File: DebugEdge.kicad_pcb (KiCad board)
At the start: 2 copper layers, 16 x 12 mm, 5 parts, among them J1 Upstream Host Connector, J2 DebugEdge_02x05, J3 BYOP

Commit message: Fix mask on bottom. Remove paste.
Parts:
- moved Ref** 6.20 mm to (162.8, 89.4)
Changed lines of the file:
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@@
   (title_block
     (title "DebugEdge Adapter")
-    (date 2020-08-26)
+    (date 2020-08-27)
     (rev 1)
     (company debug-edge.io)
-    (comment 1 "Based on @GregDavill's and @tannewt's idea!")
+    (comment 1 "Brainchild of @tannewt, @_nitz, and @GregDavill")
   )
   (layers
@@
     (fp_line (start -2.75 0.25) (end -2.75 1) (layer F.SilkS) (width 0.12))
     (fp_arc (start -1 2.8) (end -1.3 2.8) (angle -180) (layer Edge.Cuts) (width 0.05))
-    (pad 9 smd rect (at 4 2.5 270) (size 1 4) (layers F.Cu F.Paste F.Mask)
+    (pad 9 smd rect (at 4 2.5 270) (size 1 4) (layers F.Cu F.Mask)
       (net 8 "Net-(J1-Pad9)"))
-    (pad 5 smd rect (at 2 2.5 270) (size 1 4) (layers F.Cu F.Paste F.Mask)
+    (pad 5 smd rect (at 2 2.5 270) (size 1 4) (layers F.Cu F.Mask)
       (net 11 "Net-(J2-Pad5)"))
-    (pad 2 smd rect (at 0 2.5 270) (size 1 4) (layers F.Cu F.Paste F.Mask)
+    (pad 2 smd rect (at 0 2.5 270) (size 1 4) (layers F.Cu F.Mask)
       (net 4 /SWDIO))
-    (pad 1 smd rect (at -2 2.5 270) (size 1 4) (layers F.Cu F.Paste F.Mask)
+    (pad 1 smd rect (at -2 2.5 270) (size 1 4) (layers F.Cu F.Mask)
       (net 2 GND))
-    (pad 7 smd rect (at -4 2.5 270) (size 1 4) (layers F.Cu F.Paste F.Mask)
+    (pad 7 smd rect (at -4 2.5 270) (size 1 4) (layers F.Cu F.Mask)
       (net 6 "Net-(J1-Pad7)"))
-    (pad 10 smd rect (at 4 2.5 270) (size 1 4) (layers B.Cu F.Paste F.Mask)
+    (pad 10 smd rect (at 4 2.5 270) (size 1 4) (layers B.Cu B.Mask)
       (net 7 "Net-(J1-Pad10)"))
-    (pad 6 smd rect (at 2 2.5 270) (size 1 4) (layers B.Cu F.Paste F.Mask)
+    (pad 6 smd rect (at 2 2.5 270) (size 1 4) (layers B.Cu B.Mask)
       (net 10 "Net-(J1-Pad6)"))
-    (pad 3 smd rect (at -2 2.5 270) (size 1 4) (layers B.Cu F.Paste F.Mask)
+    (pad 3 smd rect (at -2 2.5 270) (size 1 4) (layers B.Cu B.Mask)
       (net 3 /SWCLK))
-    (pad 8 smd rect (at -4 2.5 270) (size 1 4) (layers B.Cu F.Paste F.Mask)
+    (pad 8 smd rect (at -4 2.5 270) (size 1 4) (layers B.Cu B.Mask)
       (net 9 "Net-(J1-Pad8)"))
-    (pad 4 smd rect (at 0 2.5 270) (size 1 4) (layers B.Cu F.Paste F.Mask)
+    (pad 4 smd rect (at 0 2.5 270) (size 1 4) (layers B.Cu B.Mask)
       (net 1 /~RESET~))
   )
   (module Connector_DebugEdge:DebugEdge_URL_Silk (layer B.Cu)
-    (at 162.8 95.6 180)
+    (at 162.8 89.4 180)
     (fp_text reference Ref** (at 0 0) (layer B.SilkS) hide
       (effects (font (size 1.27 1.27) (thickness 0.15)) (justify mirror))
@@
     )
   )
-  (gr_text "Revision 1" (at 162.2 97) (layer B.SilkS)
+  (gr_text "Revision 1" (at 160.4 90.7) (layer B.SilkS)
     (effects (font (size 1 1) (thickness 0.15)) (justify mirror))
   )

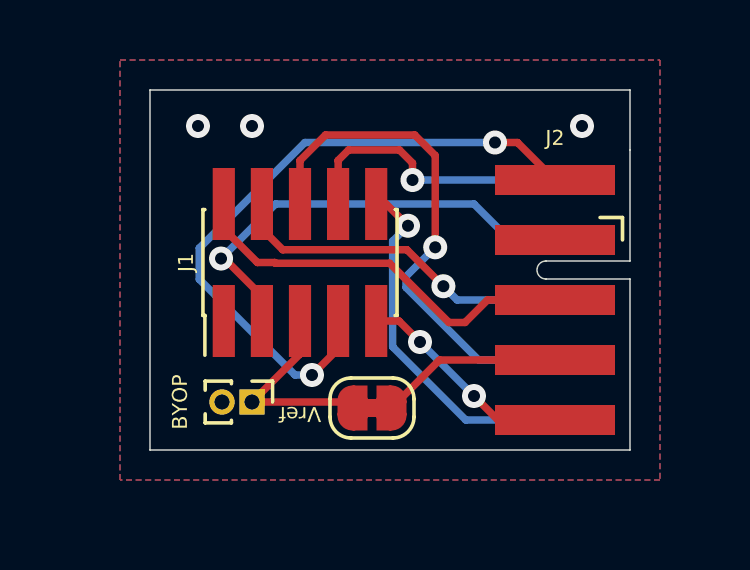
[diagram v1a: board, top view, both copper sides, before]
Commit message: Expanded edge to let ground pour flow.
And rounded the corners, cause why not?
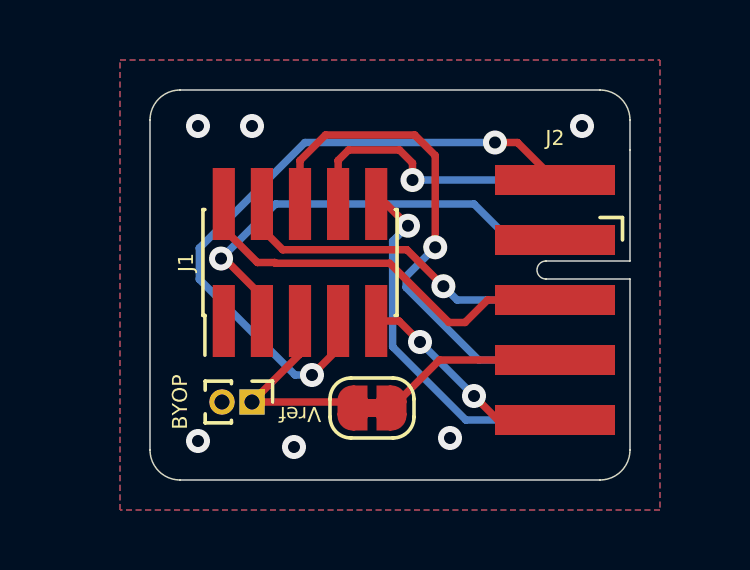
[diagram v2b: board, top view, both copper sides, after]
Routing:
- net GND: vias 3 -> 6
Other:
- board size 16 x 12 mm -> 16 x 13 mm

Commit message: Expanded board.
Gives more room for a box header if one is used.
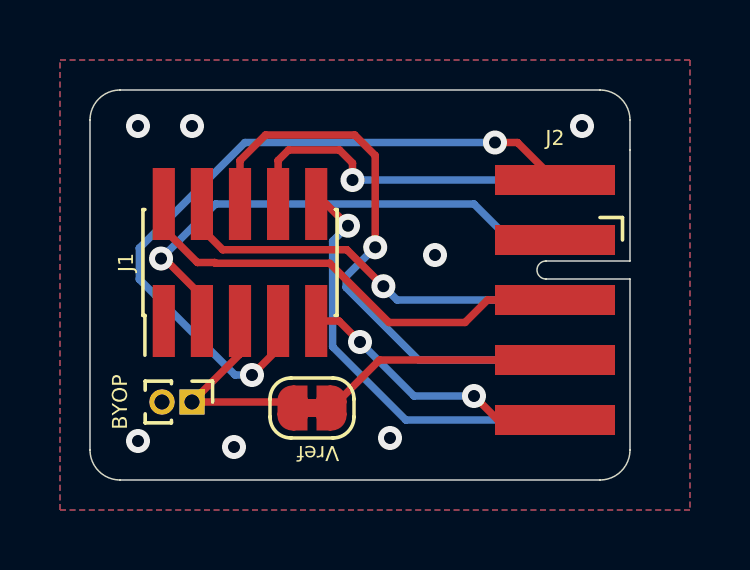
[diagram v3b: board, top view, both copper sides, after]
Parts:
- moved J1 2.00 mm to (157.0, 93.8)
- moved J3 2.00 mm to (155.4, 98.4)
- moved JP1 2.00 mm to (159.4, 98.6)
- moved Ref** 1.80 mm to (161.0, 89.5)
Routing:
- net Net-(J1-Pad7): track 22.1 -> 24.1 mm
- net Net-(J1-Pad9): track 7.33 -> 9.33 mm
- net Net-(J1-Pad6): track 17.4 -> 19.4 mm
- net Net-(J1-Pad10): track 12.1 -> 14.1 mm
- net /~RESET~: track 11.6 -> 13.6 mm
- net /SWDIO: track 13.5 -> 15.5 mm
- net /SWCLK: track 15.1 -> 17.1 mm
- net GND: vias 6 -> 7
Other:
- board size 16 x 13 mm -> 18 x 13 mm
